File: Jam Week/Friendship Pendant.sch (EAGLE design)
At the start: 39 parts, among them IC1 LM556D, IC2 LM556D, IC3 74AHC1G32DCK, U1 3039

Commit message: Almost done,
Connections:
- removed net N$26: R19.1
- removed net N$32: R17.1
- net BLINK: now also R17.1, R19.1
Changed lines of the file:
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@@
 <?xml version="1.0" encoding="utf-8"?>
 <!DOCTYPE eagle SYSTEM "eagle.dtd">
-<eagle version="9.4.0">
+<eagle version="9.5.1">
 <drawing>
 <settings>
@@
 <instance part="X_10" gate="G$1" x="-15.24" y="45.72" smashed="yes"/>
 <instance part="X_4" gate="G$1" x="127" y="-43.18" smashed="yes"/>
-<instance part="X_2" gate="G$1" x="-58.42" y="-10.16" smashed="yes"/>
+<instance part="X_2" gate="G$1" x="-58.42" y="-15.24" smashed="yes"/>
 <instance part="U1" gate="G$1" x="-58.42" y="35.56" smashed="yes" rot="R270">
 <attribute name="NAME" x="-50.8" y="-6.35" size="1.778" layer="95" rot="R270" align="center-left"/>
@@
 <attribute name="VALUE" x="-17.78" y="66.04" size="1.778" layer="96" rot="R90"/>
 </instance>
-<instance part="P+3" gate="VCC" x="-10.16" y="33.02" smashed="yes">
-<attribute name="VALUE" x="-12.7" y="30.48" size="1.778" layer="96" rot="R90"/>
+<instance part="P+3" gate="VCC" x="-10.16" y="35.56" smashed="yes">
+<attribute name="VALUE" x="-12.7" y="33.02" size="1.778" layer="96" rot="R90"/>
 </instance>
 <instance part="P+4" gate="VCC" x="-10.16" y="-15.24" smashed="yes">
 <attribute name="VALUE" x="-12.7" y="-17.78" size="1.778" layer="96" rot="R90"/>
 </instance>
-<instance part="P+5" gate="VCC" x="81.28" y="7.62" smashed="yes">
-<attribute name="VALUE" x="78.74" y="5.08" size="1.778" layer="96" rot="R90"/>
+<instance part="P+5" gate="VCC" x="83.82" y="7.62" smashed="yes">
+<attribute name="VALUE" x="81.28" y="5.08" size="1.778" layer="96" rot="R90"/>
 </instance>
 <instance part="P+6" gate="VCC" x="139.7" y="2.54" smashed="yes">
@@
 <attribute name="VALUE" x="139.7" y="68.58" size="1.778" layer="96" rot="R90"/>
 </instance>
-<instance part="P+10" gate="VCC" x="45.72" y="55.88" smashed="yes" rot="R90">
-<attribute name="VALUE" x="48.26" y="53.34" size="1.778" layer="96" rot="R180"/>
+<instance part="P+10" gate="VCC" x="45.72" y="66.04" smashed="yes">
+<attribute name="VALUE" x="43.18" y="63.5" size="1.778" layer="96" rot="R90"/>
 </instance>
 </instances>
@@
 </segment>
 <segment>
-<pinref part="IC1" gate="A" pin="GND"/>
 <wire x1="48.26" y1="30.48" x2="48.26" y2="45.72" width="0.1524" layer="91"/>
-<wire x1="48.26" y1="45.72" x2="50.8" y2="45.72" width="0.1524" layer="91"/>
 <pinref part="X_9" gate="G$1" pin="0"/>
 <wire x1="68.58" y1="30.48" x2="48.26" y2="30.48" width="0.1524" layer="91"/>
@@
 <pinref part="C6" gate="G$1" pin="2"/>
 <wire x1="86.36" y1="30.48" x2="86.36" y2="33.02" width="0.1524" layer="91"/>
+<pinref part="IC1" gate="A" pin="GND"/>
+<wire x1="50.8" y1="45.72" x2="48.26" y2="45.72" width="0.1524" layer="91"/>
 </segment>
 <segment>
@@
 <pinref part="U1" gate="G$1" pin="NEGATIVE_CONTACT_PAD"/>
 <pinref part="X_2" gate="G$1" pin="0"/>
+<wire x1="-58.42" y1="-15.24" x2="-58.42" y2="-10.16" width="0.1524" layer="91"/>
 </segment>
 </net>
@@
 <pinref part="R9" gate="G$1" pin="1"/>
 <pinref part="P+3" gate="VCC" pin="VCC"/>
+<wire x1="-10.16" y1="33.02" x2="-10.16" y2="30.48" width="0.1524" layer="91"/>
 </segment>
 <segment>
@@
 <wire x1="-10.16" y1="-20.32" x2="-10.16" y2="-17.78" width="0.1524" layer="91"/>
 <pinref part="P+4" gate="VCC" pin="VCC"/>
+</segment>
+<segment>
+<pinref part="R16" gate="G$1" pin="1"/>
+<wire x1="139.7" y1="-2.54" x2="139.7" y2="0" width="0.1524" layer="91"/>
+<pinref part="P+6" gate="VCC" pin="VCC"/>
+</segment>
+<segment>
+<pinref part="Q5" gate="G$1" pin="E"/>
+<wire x1="180.34" y1="-10.16" x2="180.34" y2="-12.7" width="0.1524" layer="91"/>
+<pinref part="P+7" gate="VCC" pin="VCC"/>
+</segment>
+<segment>
+<pinref part="R11" gate="G$1" pin="2"/>
+<wire x1="180.34" y1="60.96" x2="180.34" y2="63.5" width="0.1524" layer="91"/>
+<pinref part="P+8" gate="VCC" pin="VCC"/>
+</segment>
+<segment>
+<pinref part="R2" gate="G$1" pin="2"/>
+<wire x1="142.24" y1="63.5" x2="142.24" y2="68.58" width="0.1524" layer="91"/>
+<pinref part="P+9" gate="VCC" pin="VCC"/>
+</segment>
+<segment>
+<pinref part="P+10" gate="VCC" pin="VCC"/>
+<wire x1="45.72" y1="63.5" x2="45.72" y2="55.88" width="0.1524" layer="91"/>
+<pinref part="IC1" gate="A" pin="R"/>
+<wire x1="45.72" y1="55.88" x2="50.8" y2="55.88" width="0.1524" layer="91"/>
 </segment>
 <segment>
@@
 <wire x1="78.74" y1="-20.32" x2="78.74" y2="2.54" width="0.1524" layer="91"/>
 <pinref part="R6" gate="G$1" pin="2"/>
-<wire x1="78.74" y1="2.54" x2="81.28" y2="2.54" width="0.1524" layer="91"/>
-<wire x1="81.28" y1="2.54" x2="83.82" y2="2.54" width="0.1524" layer="91"/>
-<wire x1="81.28" y1="5.08" x2="81.28" y2="2.54" width="0.1524" layer="91"/>
-<junction x="81.28" y="2.54"/>
+<wire x1="78.74" y1="2.54" x2="83.82" y2="2.54" width="0.1524" layer="91"/>
 <pinref part="P+5" gate="VCC" pin="VCC"/>
-</segment>
-<segment>
-<pinref part="R16" gate="G$1" pin="1"/>
-<wire x1="139.7" y1="-2.54" x2="139.7" y2="0" width="0.1524" layer="91"/>
-<pinref part="P+6" gate="VCC" pin="VCC"/>
-</segment>
-<segment>
-<pinref part="Q5" gate="G$1" pin="E"/>
-<wire x1="180.34" y1="-10.16" x2="180.34" y2="-12.7" width="0.1524" layer="91"/>
-<pinref part="P+7" gate="VCC" pin="VCC"/>
-</segment>
-<segment>
-<pinref part="R11" gate="G$1" pin="2"/>
-<wire x1="180.34" y1="60.96" x2="180.34" y2="63.5" width="0.1524" layer="91"/>
-<pinref part="P+8" gate="VCC" pin="VCC"/>
-</segment>
-<segment>
-<pinref part="R2" gate="G$1" pin="2"/>
-<wire x1="142.24" y1="63.5" x2="142.24" y2="68.58" width="0.1524" layer="91"/>
-<pinref part="P+9" gate="VCC" pin="VCC"/>
-</segment>
-<segment>
-<pinref part="IC1" gate="A" pin="R"/>
-<wire x1="50.8" y1="55.88" x2="48.26" y2="55.88" width="0.1524" layer="91"/>
-<pinref part="P+10" gate="VCC" pin="VCC"/>
+<wire x1="83.82" y1="5.08" x2="83.82" y2="2.54" width="0.1524" layer="91"/>
+<junction x="83.82" y="2.54"/>
 </segment>
 </net>
@@
 <wire x1="132.08" y1="58.42" x2="132.08" y2="68.58" width="0.1524" layer="91"/>
 <label x="132.08" y="68.58" size="1.778" layer="95" rot="R90" xref="yes"/>
+</segment>
+<segment>
+<pinref part="R19" gate="G$1" pin="1"/>
+<wire x1="165.1" y1="38.1" x2="162.56" y2="38.1" width="0.1524" layer="91"/>
 <label x="162.56" y="38.1" size="1.778" layer="95" rot="R180" xref="yes"/>
+</segment>
+<segment>
+<pinref part="R17" gate="G$1" pin="1"/>
+<wire x1="165.1" y1="-17.78" x2="162.56" y2="-17.78" width="0.1524" layer="91"/>
 <label x="162.56" y="-17.78" size="1.778" layer="95" rot="R180" xref="yes"/>
 </segment>
@@
 </segment>
 </net>
-<net name="N$26" class="0">
-<segment>
-<pinref part="R19" gate="G$1" pin="1"/>
-<wire x1="165.1" y1="38.1" x2="162.56" y2="38.1" width="0.1524" layer="91"/>
-</segment>
-</net>
-<net name="N$32" class="0">
-<segment>
-<pinref part="R17" gate="G$1" pin="1"/>
-<wire x1="165.1" y1="-17.78" x2="162.56" y2="-17.78" width="0.1524" layer="91"/>
-</segment>
-</net>

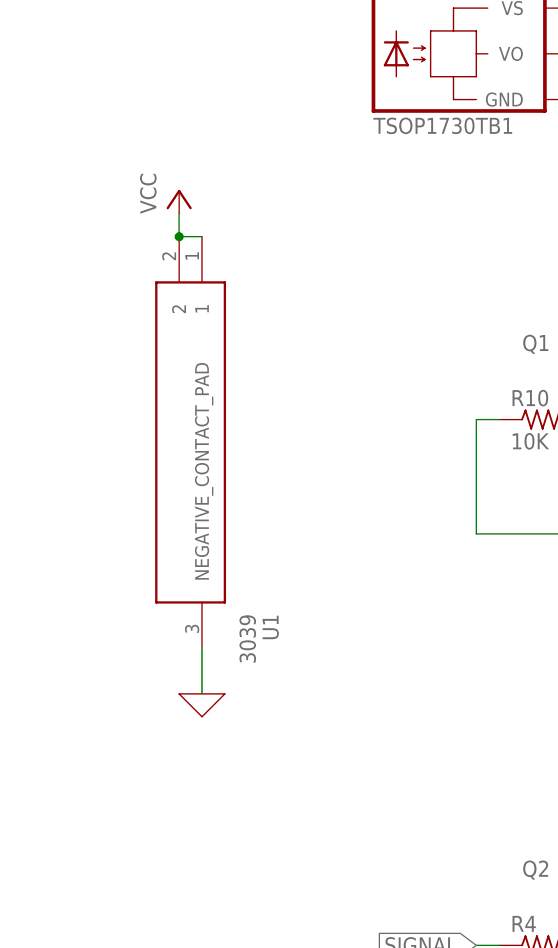
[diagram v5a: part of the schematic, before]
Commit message: added switch and ordered without switch
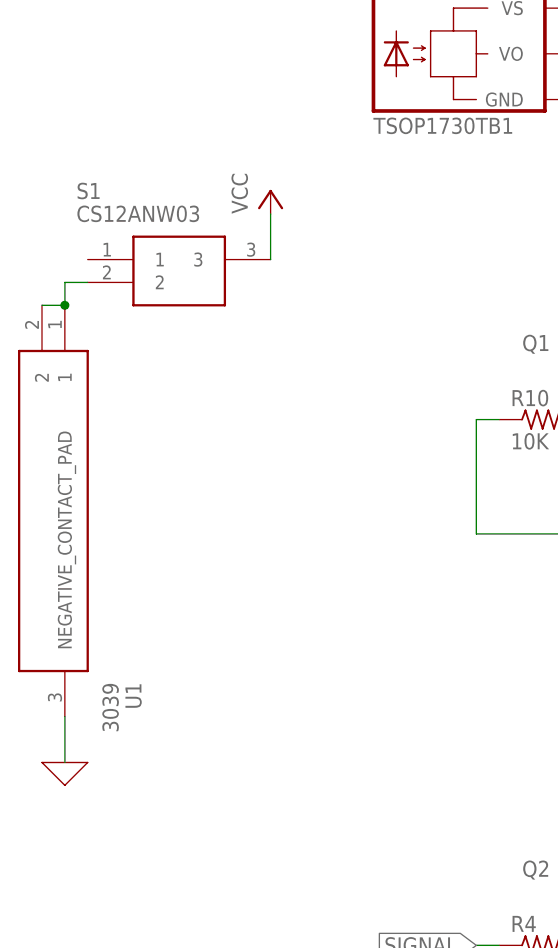
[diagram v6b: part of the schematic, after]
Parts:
- added S1: CS12ANW03, CS12ANW03:CS12ANW03
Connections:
- new net N$15: S1.2, U1.1, U1.2
- net VCC: now also S1.3; no longer U1.1, U1.2
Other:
- moved on the sheet: U1
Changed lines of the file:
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@@
 <part name="P+9" library="supply1" library_urn="urn:adsk.eagle:library:371" deviceset="VCC" device=""/>
 <part name="P+10" library="supply1" library_urn="urn:adsk.eagle:library:371" deviceset="VCC" device=""/>
+<part name="S1" library="CS12ANW03" deviceset="CS12ANW03" device=""/>
 </parts>
 <sheets>
@@
 <instance part="X_10" gate="G$1" x="-15.24" y="45.72" smashed="yes"/>
 <instance part="X_4" gate="G$1" x="127" y="-43.18" smashed="yes"/>
-<instance part="X_2" gate="G$1" x="-58.42" y="-15.24" smashed="yes"/>
-<instance part="U1" gate="G$1" x="-58.42" y="35.56" smashed="yes" rot="R270">
-<attribute name="NAME" x="-50.8" y="-6.35" size="1.778" layer="95" rot="R270" align="center-left"/>
-<attribute name="VALUE" x="-53.34" y="-6.35" size="1.778" layer="96" rot="R270" align="center-left"/>
-</instance>
-<instance part="P+1" gate="VCC" x="-60.96" y="40.64" smashed="yes">
-<attribute name="VALUE" x="-63.5" y="38.1" size="1.778" layer="96" rot="R90"/>
+<instance part="X_2" gate="G$1" x="-73.66" y="-22.86" smashed="yes"/>
+<instance part="U1" gate="G$1" x="-73.66" y="27.94" smashed="yes" rot="R270">
+<attribute name="NAME" x="-66.04" y="-13.97" size="1.778" layer="95" rot="R270" align="center-left"/>
+<attribute name="VALUE" x="-68.58" y="-13.97" size="1.778" layer="96" rot="R270" align="center-left"/>
+</instance>
+<instance part="P+1" gate="VCC" x="-50.8" y="40.64" smashed="yes">
+<attribute name="VALUE" x="-53.34" y="38.1" size="1.778" layer="96" rot="R90"/>
 </instance>
 <instance part="P+2" gate="VCC" x="-15.24" y="68.58" smashed="yes">
@@
 <instance part="P+10" gate="VCC" x="45.72" y="66.04" smashed="yes">
 <attribute name="VALUE" x="43.18" y="63.5" size="1.778" layer="96" rot="R90"/>
+</instance>
+<instance part="S1" gate="G$1" x="-71.12" y="33.02" smashed="yes">
+<attribute name="NAME" x="-72.39" y="40.64" size="1.778" layer="95" align="center-left"/>
+<attribute name="VALUE" x="-72.39" y="38.1" size="1.778" layer="96" align="center-left"/>
 </instance>
 </instances>
@@
 <pinref part="U1" gate="G$1" pin="NEGATIVE_CONTACT_PAD"/>
 <pinref part="X_2" gate="G$1" pin="0"/>
-<wire x1="-58.42" y1="-15.24" x2="-58.42" y2="-10.16" width="0.1524" layer="91"/>
+<wire x1="-73.66" y1="-22.86" x2="-73.66" y2="-17.78" width="0.1524" layer="91"/>
 </segment>
 </net>
@@
 </segment>
 <segment>
-<pinref part="U1" gate="G$1" pin="1"/>
-<pinref part="U1" gate="G$1" pin="2"/>
-<wire x1="-58.42" y1="35.56" x2="-60.96" y2="35.56" width="0.1524" layer="91"/>
-<wire x1="-60.96" y1="38.1" x2="-60.96" y2="35.56" width="0.1524" layer="91"/>
-<junction x="-60.96" y="35.56"/>
-<pinref part="P+1" gate="VCC" pin="VCC"/>
-</segment>
-<segment>
 <pinref part="R9" gate="G$1" pin="1"/>
 <pinref part="P+3" gate="VCC" pin="VCC"/>
@@
 <wire x1="83.82" y1="5.08" x2="83.82" y2="2.54" width="0.1524" layer="91"/>
 <junction x="83.82" y="2.54"/>
+</segment>
+<segment>
+<pinref part="S1" gate="G$1" pin="3"/>
+<pinref part="P+1" gate="VCC" pin="VCC"/>
+<wire x1="-50.8" y1="33.02" x2="-50.8" y2="38.1" width="0.1524" layer="91"/>
 </segment>
 </net>
@@
 </segment>
 </net>
+<net name="N$15" class="0">
+<segment>
+<pinref part="U1" gate="G$1" pin="1"/>
+<pinref part="U1" gate="G$1" pin="2"/>
+<wire x1="-73.66" y1="27.94" x2="-76.2" y2="27.94" width="0.1524" layer="91"/>
+<wire x1="-73.66" y1="27.94" x2="-73.66" y2="30.48" width="0.1524" layer="91"/>
+<junction x="-73.66" y="27.94"/>
+<pinref part="S1" gate="G$1" pin="2"/>
+<wire x1="-73.66" y1="30.48" x2="-71.12" y2="30.48" width="0.1524" layer="91"/>
+</segment>
+</net>

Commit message: Updated some parts before ordering from Mouser
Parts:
- IC1, IC2: MOUSER# (none) -> 511-TS556IDTTR; MPN (none) -> TS556IDTTR
- Q5: MOUSER# (none) -> 583-BC856A-T; MPN (none) -> BC856A-T
- U1: MOUSER# (none) -> 534-3039; MPN (none) -> 3039
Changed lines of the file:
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@@
 <?xml version="1.0" encoding="utf-8"?>
 <!DOCTYPE eagle SYSTEM "eagle.dtd">
-<eagle version="9.5.1">
+<eagle version="9.2.2">
 <drawing>
 <settings>
@@
 </classes>
 <parts>
-<part name="IC1" library="linear" library_urn="urn:adsk.eagle:library:262" deviceset="*556" device="D" package3d_urn="urn:adsk.eagle:package:16406/2" technology="LM"/>
-<part name="IC2" library="linear" library_urn="urn:adsk.eagle:library:262" deviceset="*556" device="D" package3d_urn="urn:adsk.eagle:package:16406/2" technology="LM"/>
+<part name="IC1" library="linear" library_urn="urn:adsk.eagle:library:262" deviceset="*556" device="D" package3d_urn="urn:adsk.eagle:package:16406/2" technology="LM">
+<attribute name="MOUSER#" value="511-TS556IDTTR
+"/>
+<attribute name="MPN" value="TS556IDTTR
+"/>
+</part>
+<part name="IC2" library="linear" library_urn="urn:adsk.eagle:library:262" deviceset="*556" device="D" package3d_urn="urn:adsk.eagle:package:16406/2" technology="LM">
+<attribute name="MOUSER#" value="511-TS556IDTTR
+"/>
+<attribute name="MPN" value="TS556IDTTR
+"/>
+</part>
 <part name="R1" library="rcl" library_urn="urn:adsk.eagle:library:334" deviceset="R-US_" device="R0805" package3d_urn="urn:adsk.eagle:package:23553/2" value="28.7K">
 <spice>
@@
 <attribute name="SPICEPREFIX" value="Q"/>
 </part>
-<part name="Q5" library="semicon-smd-ipc" library_urn="urn:adsk.eagle:library:353" deviceset="PNP-TRANSISTOR_" device="SOT23" package3d_urn="urn:adsk.eagle:package:26310/1"/>
+<part name="Q5" library="semicon-smd-ipc" library_urn="urn:adsk.eagle:library:353" deviceset="PNP-TRANSISTOR_" device="SOT23" package3d_urn="urn:adsk.eagle:package:26310/1">
+<attribute name="MOUSER#" value="583-BC856A-T
+"/>
+<attribute name="MPN" value="BC856A-T
+"/>
+</part>
 <part name="LED1" library="led" library_urn="urn:adsk.eagle:library:259" deviceset="LED" device="IRL80A" package3d_urn="urn:adsk.eagle:package:15810/1">
 <attribute name="MOUSER#" value="782-TSAL6200"/>
@@
 <part name="X_4" library="ngspice-simulation" library_urn="urn:adsk.eagle:library:527439" deviceset="GND" device=""/>
 <part name="X_2" library="ngspice-simulation" library_urn="urn:adsk.eagle:library:527439" deviceset="GND" device=""/>
-<part name="U1" library="3039" deviceset="3039" device=""/>
+<part name="U1" library="3039" deviceset="3039" device="">
+<attribute name="MOUSER#" value="534-3039"/>
+<attribute name="MPN" value="3039"/>
+</part>
 <part name="P+1" library="supply1" library_urn="urn:adsk.eagle:library:371" deviceset="VCC" device=""/>
 <part name="P+2" library="supply1" library_urn="urn:adsk.eagle:library:371" deviceset="VCC" device=""/>
@@
 <attribute name="NAME" x="53.34" y="64.262" size="1.778" layer="95"/>
 <attribute name="VALUE" x="53.34" y="40.513" size="1.778" layer="96"/>
+<attribute name="MOUSER#" x="60.96" y="53.34" size="1.778" layer="96" display="off"/>
+<attribute name="MPN" x="60.96" y="53.34" size="1.778" layer="96" display="off"/>
 </instance>
 <instance part="IC1" gate="B" x="119.38" y="53.34" smashed="yes">
@@
 <attribute name="NAME" x="53.34" y="-1.778" size="1.778" layer="95"/>
 <attribute name="VALUE" x="53.34" y="-25.527" size="1.778" layer="96"/>
+<attribute name="MOUSER#" x="60.96" y="-12.7" size="1.778" layer="96" display="off"/>
+<attribute name="MPN" x="60.96" y="-12.7" size="1.778" layer="96" display="off"/>
 </instance>
 <instance part="IC2" gate="B" x="119.38" y="-12.7" smashed="yes">
@@
 <attribute name="NAME" x="167.64" y="-10.16" size="1.778" layer="95"/>
 <attribute name="VALUE" x="167.64" y="-12.7" size="1.778" layer="96"/>
+<attribute name="MOUSER#" x="177.8" y="-17.78" size="1.778" layer="96" display="off"/>
+<attribute name="MPN" x="177.8" y="-17.78" size="1.778" layer="96" display="off"/>
 </instance>
 <instance part="LED1" gate="G$1" x="-10.16" y="-33.02" smashed="yes">
@@
 <attribute name="NAME" x="-66.04" y="-13.97" size="1.778" layer="95" rot="R270" align="center-left"/>
 <attribute name="VALUE" x="-68.58" y="-13.97" size="1.778" layer="96" rot="R270" align="center-left"/>
+<attribute name="MOUSER#" x="-73.66" y="27.94" size="1.778" layer="96" rot="R270" display="off"/>
+<attribute name="MPN" x="-73.66" y="27.94" size="1.778" layer="96" rot="R270" display="off"/>
 </instance>
 <instance part="P+1" gate="VCC" x="-50.8" y="40.64" smashed="yes">

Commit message: final day
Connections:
- net 0: now also IC3P.GND
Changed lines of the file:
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@@
 <?xml version="1.0" encoding="utf-8"?>
 <!DOCTYPE eagle SYSTEM "eagle.dtd">
-<eagle version="9.2.2">
+<eagle version="9.5.1">
 <drawing>
 <settings>
@@
 <parts>
 <part name="IC1" library="linear" library_urn="urn:adsk.eagle:library:262" deviceset="*556" device="D" package3d_urn="urn:adsk.eagle:package:16406/2" technology="LM">
-<attribute name="MOUSER#" value="511-TS556IDTTR
-"/>
-<attribute name="MPN" value="TS556IDTTR
-"/>
+<attribute name="MOUSER#" value="511-TS556IDTTR "/>
+<attribute name="MPN" value="TS556IDTTR "/>
 </part>
 <part name="IC2" library="linear" library_urn="urn:adsk.eagle:library:262" deviceset="*556" device="D" package3d_urn="urn:adsk.eagle:package:16406/2" technology="LM">
-<attribute name="MOUSER#" value="511-TS556IDTTR
-"/>
-<attribute name="MPN" value="TS556IDTTR
-"/>
+<attribute name="MOUSER#" value="511-TS556IDTTR "/>
+<attribute name="MPN" value="TS556IDTTR "/>
 </part>
 <part name="R1" library="rcl" library_urn="urn:adsk.eagle:library:334" deviceset="R-US_" device="R0805" package3d_urn="urn:adsk.eagle:package:23553/2" value="28.7K">
@@
 </part>
 <part name="Q5" library="semicon-smd-ipc" library_urn="urn:adsk.eagle:library:353" deviceset="PNP-TRANSISTOR_" device="SOT23" package3d_urn="urn:adsk.eagle:package:26310/1">
-<attribute name="MOUSER#" value="583-BC856A-T
-"/>
-<attribute name="MPN" value="BC856A-T
-"/>
+<attribute name="MOUSER#" value="583-BC856A-T "/>
+<attribute name="MPN" value="BC856A-T "/>
 </part>
 <part name="LED1" library="led" library_urn="urn:adsk.eagle:library:259" deviceset="LED" device="IRL80A" package3d_urn="urn:adsk.eagle:package:15810/1">
@@
 <part name="P+10" library="supply1" library_urn="urn:adsk.eagle:library:371" deviceset="VCC" device=""/>
 <part name="S1" library="CS12ANW03" deviceset="CS12ANW03" device=""/>
+<part name="X_11" library="ngspice-simulation" library_urn="urn:adsk.eagle:library:527439" deviceset="GND" device=""/>
 </parts>
 <sheets>
@@
 <attribute name="VALUE" x="-72.39" y="38.1" size="1.778" layer="96" align="center-left"/>
 </instance>
+<instance part="IC3" gate="P" x="15.24" y="53.34" smashed="yes">
+<attribute name="NAME" x="14.605" y="52.705" size="1.778" layer="95"/>
+</instance>
+<instance part="X_11" gate="G$1" x="15.24" y="43.18" smashed="yes"/>
 </instances>
 <busses>
@@
 <wire x1="-73.66" y1="-22.86" x2="-73.66" y2="-17.78" width="0.1524" layer="91"/>
 </segment>
-</net>
+<segment>
+<pinref part="X_11" gate="G$1" pin="0"/>
+<pinref part="IC3" gate="P" pin="GND"/>
+<wire x1="15.24" y1="43.18" x2="15.24" y2="45.72" width="0.1524" layer="91"/>
+</segment>
+</net>
